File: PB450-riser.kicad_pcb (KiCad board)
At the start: 2 copper layers, 160 x 81.3 mm, 3 parts, among them J1 J1, J2 J2

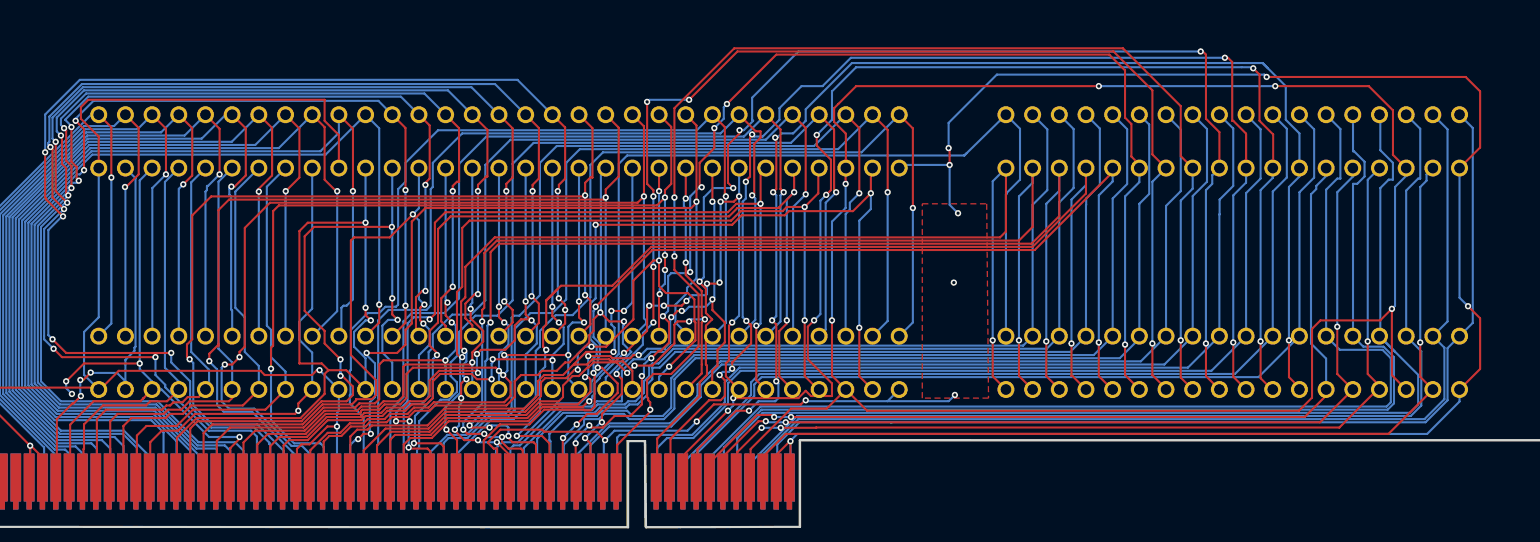
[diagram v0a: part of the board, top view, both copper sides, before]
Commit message: upload footprint for isa slot
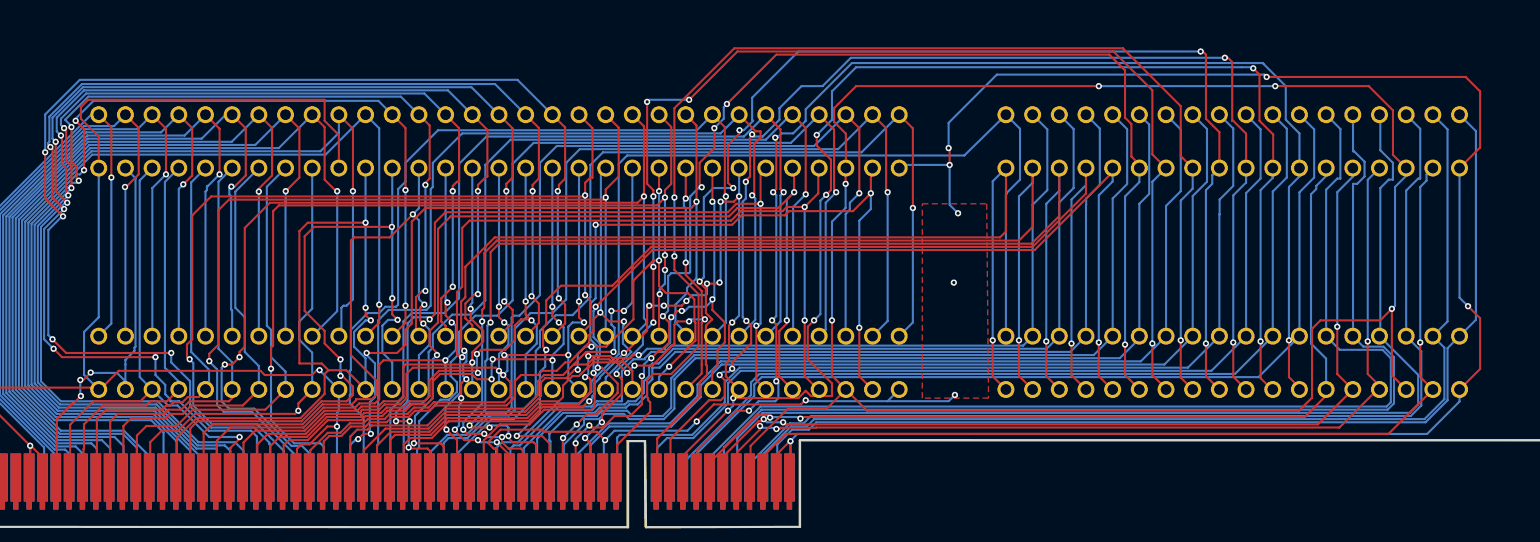
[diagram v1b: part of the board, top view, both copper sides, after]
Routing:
- net VCC: track 246.5 -> 237.4 mm, vias 9 -> 6
- net (no net): track 7616.4 -> 7612.3 mm, vias 242 -> 239

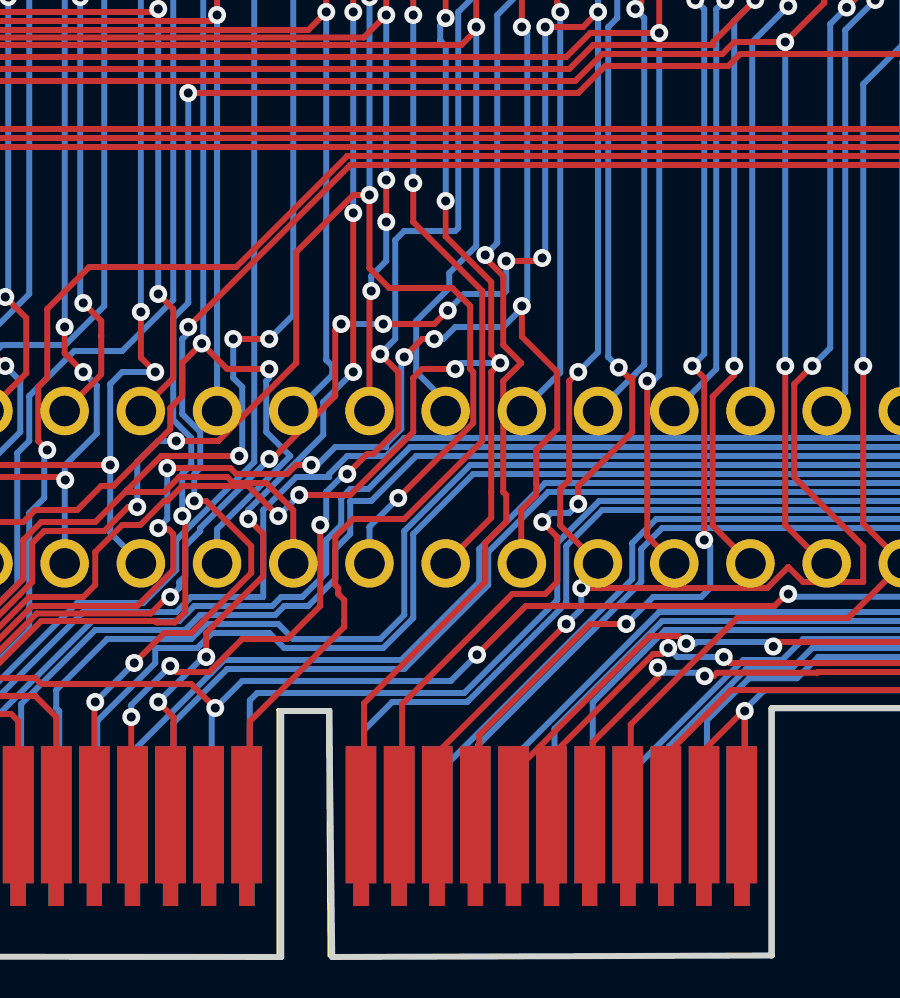
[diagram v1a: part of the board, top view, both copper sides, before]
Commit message: correcting for DRC
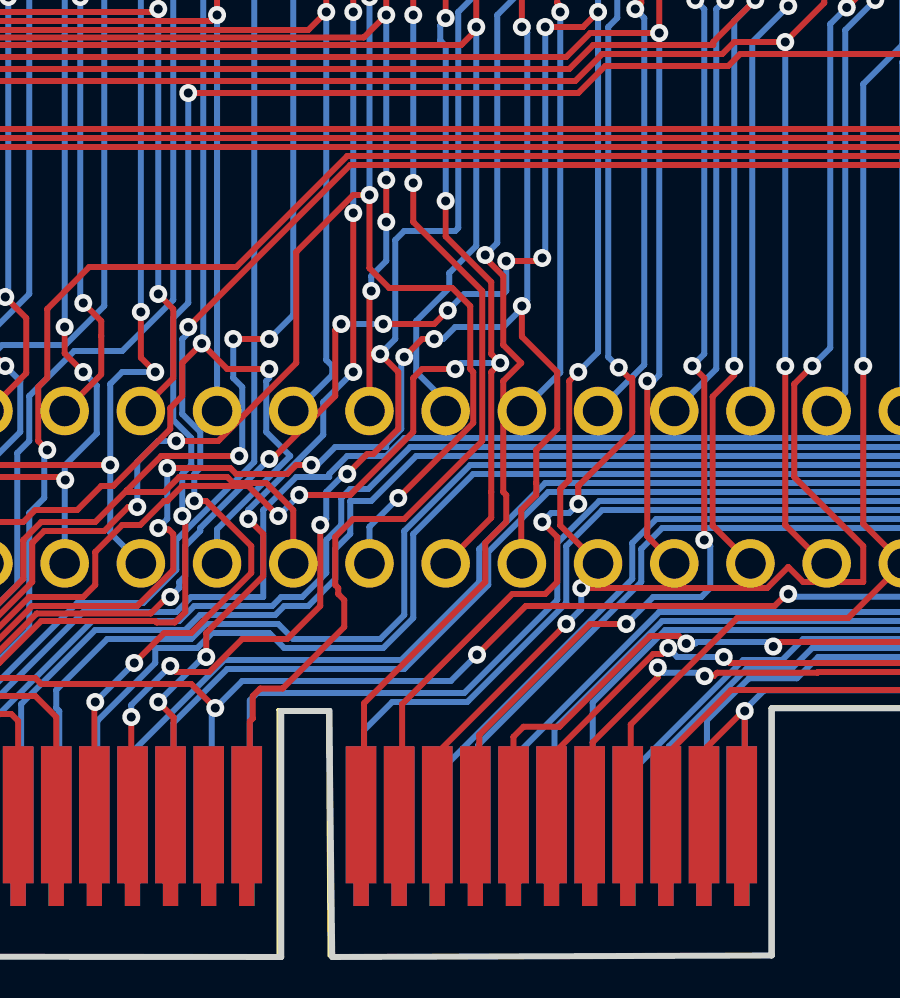
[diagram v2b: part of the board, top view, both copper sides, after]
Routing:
- net (no net): track 7612.3 -> 7615.0 mm

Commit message: revisions and adding foot prints
revisions and adding footprints
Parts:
- added P2: PCI 32bit footprint (partial), Connector_PCBEdge:BUS_PCI, F.Cu at (139.3, 92.7)
- J2: value J2 -> J1
- P1: renamed from REF**; value BUS_PCI -> ISA Bus over PCI; footprint Connector_PCBEdge:BUS_PCI -> Connector_PCBEdge:BUS_ISA-over-PCI
- moved J2 8.92 mm to (108.0, 116.6)
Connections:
- J1 pad A1: (no net) -> Net-(J1-~{IO_CH_CK})
- J1 pad A10: (no net) -> Net-(J1-IO_CH_RDY)
- J1 pad A11: (no net) -> Net-(J1-AEN)
- J1 pad A12: (no net) -> /SA19
- J1 pad A13: (no net) -> /SA18
- J1 pad A14: (no net) -> /SA17
- J1 pad A15: (no net) -> /SA16
- J1 pad A16: (no net) -> /SA15
- J1 pad A17: (no net) -> /SA14
- J1 pad A18: (no net) -> /SA13
- J1 pad A19: (no net) -> /SA12
- J1 pad A2: (no net) -> /SD7
- J1 pad A20: (no net) -> /SA11
- J1 pad A21: (no net) -> /SA10
- J1 pad A22: (no net) -> /SA9
- J1 pad A23: (no net) -> /SA8
- J1 pad A24: (no net) -> /SA7
- J1 pad A25: (no net) -> /SA6
- J1 pad A26: (no net) -> /SA5
- J1 pad A27: (no net) -> /SA4
- J1 pad A28: (no net) -> /SA3
- J1 pad A29: (no net) -> /SA2
- J1 pad A3: (no net) -> /SD6
- J1 pad A30: (no net) -> /SA1
- J1 pad A31: (no net) -> /SA0
- J1 pad A4: (no net) -> /SD5
- J1 pad A5: (no net) -> /SD4
- J1 pad A6: (no net) -> /SD3
- J1 pad A7: (no net) -> /SD2
- J1 pad A8: (no net) -> /SD1
- J1 pad A9: (no net) -> /SD0
- J1 pad B11: (no net) -> Net-(J1-~{SMEMW})
- J1 pad B12: (no net) -> Net-(J1-~{SMEMR})
- J1 pad B13: (no net) -> Net-(J1-~{IOW})
- J1 pad B14: (no net) -> Net-(J1-~{IOR})
- J1 pad B15: (no net) -> Net-(J1-~{DACK3})
- J1 pad B16: (no net) -> Net-(J1-DRQ3)
- J1 pad B17: (no net) -> Net-(J1-~{DACK1})
- J1 pad B18: (no net) -> Net-(J1-DRQ1)
- J1 pad B19: (no net) -> Net-(J1-~{REFRESH})
- J1 pad B2: (no net) -> Net-(J1-RESETDRV)
- J1 pad B20: (no net) -> Net-(J1-SYSCLK)
- J1 pad B21: (no net) -> Net-(J1-IRQ7)
- J1 pad B22: (no net) -> Net-(J1-IRQ6)
- J1 pad B23: (no net) -> Net-(J1-IRQ5)
- J1 pad B24: (no net) -> Net-(J1-IRQ4)
- J1 pad B25: (no net) -> Net-(J1-IRQ3)
- J1 pad B26: (no net) -> Net-(J1-~{DACK2})
- J1 pad B27: (no net) -> Net-(J1-TC)
- J1 pad B28: (no net) -> Net-(J1-BALE)
- J1 pad B29: VCC -> +5V
- J1 pad B3: VCC -> +5V
- J1 pad B30: (no net) -> Net-(J1-OSC)
- J1 pad B4: (no net) -> Net-(J1-IRQ9)
- J1 pad B6: (no net) -> Net-(J1-DRQ2)
- J1 pad B8: (no net) -> Net-(J1-~{0WS})
- J2 pad A1: (no net) -> Net-(J1-~{IO_CH_CK})
- J2 pad A10: (no net) -> Net-(J1-IO_CH_RDY)
- J2 pad A11: (no net) -> Net-(J1-AEN)
- J2 pad A12: (no net) -> /SA19
- J2 pad A13: (no net) -> /SA18
- J2 pad A14: (no net) -> /SA17
- J2 pad A15: (no net) -> /SA16
- J2 pad A16: (no net) -> /SA15
- J2 pad A17: (no net) -> /SA14
- J2 pad A18: (no net) -> /SA13
- J2 pad A19: (no net) -> /SA12
- J2 pad A2: (no net) -> /SD7
- J2 pad A20: (no net) -> /SA11
- J2 pad A21: (no net) -> /SA10
- J2 pad A22: (no net) -> /SA9
- J2 pad A23: (no net) -> /SA8
- J2 pad A24: (no net) -> /SA7
- J2 pad A25: (no net) -> /SA6
- J2 pad A26: (no net) -> /SA5
- J2 pad A27: (no net) -> /SA4
- J2 pad A28: (no net) -> /SA3
- J2 pad A29: (no net) -> /SA2
- J2 pad A3: (no net) -> /SD6
- J2 pad A30: (no net) -> /SA1
- J2 pad A31: (no net) -> /SA0
- J2 pad A4: (no net) -> /SD5
- J2 pad A5: (no net) -> /SD4
- J2 pad A6: (no net) -> /SD3
- J2 pad A7: (no net) -> /SD2
- J2 pad A8: (no net) -> /SD1
- J2 pad A9: (no net) -> /SD0
- J2 pad B1: (no net) -> GND
- J2 pad B10: (no net) -> GND
- J2 pad B11: (no net) -> Net-(J1-~{SMEMW})
- J2 pad B12: (no net) -> Net-(J1-~{SMEMR})
- J2 pad B13: (no net) -> Net-(J1-~{IOW})
- J2 pad B14: (no net) -> Net-(J1-~{IOR})
- J2 pad B15: (no net) -> Net-(J1-~{DACK3})
- J2 pad B16: (no net) -> Net-(J1-DRQ3)
- J2 pad B17: (no net) -> Net-(J1-~{DACK1})
- J2 pad B18: (no net) -> Net-(J1-DRQ1)
- J2 pad B19: (no net) -> Net-(J1-~{REFRESH})
- J2 pad B2: (no net) -> Net-(J1-RESETDRV)
- J2 pad B20: (no net) -> Net-(J1-SYSCLK)
- J2 pad B21: (no net) -> Net-(J1-IRQ7)
- J2 pad B22: (no net) -> Net-(J1-IRQ6)
- J2 pad B23: (no net) -> Net-(J1-IRQ5)
- J2 pad B24: (no net) -> Net-(J1-IRQ4)
- J2 pad B25: (no net) -> Net-(J1-IRQ3)
- J2 pad B26: (no net) -> Net-(J1-~{DACK2})
- J2 pad B27: (no net) -> Net-(J1-TC)
- J2 pad B28: (no net) -> Net-(J1-BALE)
- J2 pad B29: VCC -> +5V
- J2 pad B3: VCC -> +5V
- J2 pad B30: (no net) -> Net-(J1-OSC)
- J2 pad B4: (no net) -> Net-(J1-IRQ9)
- J2 pad B6: (no net) -> Net-(J1-DRQ2)
- J2 pad B8: (no net) -> Net-(J1-~{0WS})
- P1 pad A1: (no net) -> Net-(J1-~{IO_CH_CK})
- P1 pad A10: (no net) -> Net-(J1-IO_CH_RDY)
- P1 pad A11: (no net) -> Net-(J1-AEN)
- P1 pad A12: (no net) -> /SA19
- P1 pad A13: (no net) -> /SA18
- P1 pad A14: (no net) -> /SA17
- P1 pad A15: (no net) -> /SA16
- P1 pad A16: (no net) -> /SA15
- P1 pad A17: (no net) -> /SA14
- P1 pad A18: (no net) -> /SA13
- P1 pad A19: (no net) -> /SA12
- P1 pad A2: (no net) -> /SD7
- P1 pad A20: (no net) -> /SA11
- P1 pad A21: (no net) -> /SA10
- P1 pad A22: (no net) -> /SA9
- P1 pad A23: (no net) -> /SA8
- P1 pad A24: (no net) -> /SA7
- P1 pad A25: (no net) -> /SA6
- P1 pad A26: (no net) -> /SA5
- P1 pad A27: (no net) -> /SA4
- P1 pad A28: GND -> /SA3
- P1 pad A29: (no net) -> /SA2
- P1 pad A3: (no net) -> /SD6
- P1 pad A30: (no net) -> /SA1
- P1 pad A31: (no net) -> /SA0
- P1 pad A4: (no net) -> /SD5
- P1 pad A5: GND -> /SD4
- P1 pad A6: (no net) -> /SD3
- P1 pad A7: (no net) -> /SD2
- P1 pad A8: (no net) -> /SD1
- P1 pad A9: (no net) -> /SD0
- P1 pad B1: (no net) -> GND
- P1 pad B10: -5V -> GND
- P1 pad B11: (no net) -> Net-(J1-~{SMEMW})
- P1 pad B12: -12V -> Net-(J1-~{SMEMR})
- P1 pad B13: (no net) -> Net-(J1-~{IOW})
- P1 pad B14: +12V -> Net-(J1-~{IOR})
- P1 pad B15: (no net) -> Net-(J1-~{DACK3})
- P1 pad B16: (no net) -> Net-(J1-DRQ3)
- P1 pad B17: (no net) -> Net-(J1-~{DACK1})
- P1 pad B18: (no net) -> Net-(J1-DRQ1)
- P1 pad B2: (no net) -> Net-(J1-RESETDRV)
- P1 pad B20: VCC -> Net-(J1-~{REFRESH})
- P1 pad B21: (no net) -> Net-(J1-SYSCLK)
- P1 pad B22: (no net) -> Net-(J1-IRQ7)
- P1 pad B23: (no net) -> Net-(J1-IRQ6)
- P1 pad B24: (no net) -> Net-(J1-IRQ5)
- P1 pad B25: GND -> Net-(J1-IRQ4)
- P1 pad B26: (no net) -> Net-(J1-IRQ3)
- P1 pad B27: (no net) -> Net-(J1-~{DACK2})
- P1 pad B28: (no net) -> Net-(J1-TC)
- P1 pad B29: (no net) -> +5V
- P1 pad B3: (no net) -> +5V
- P1 pad B30: (no net) -> Net-(J1-OSC)
- P1 pad B31: (no net) -> GND
- P1 pad B4: (no net) -> Net-(J1-IRQ9)
- P1 pad B5: GND -> -5V
- P1 pad B6: GND -> Net-(J1-DRQ2)
- P1 pad B7: (no net) -> -12V
- P1 pad B8: VCC -> Net-(J1-~{0WS})
- P1 pad B9: (no net) -> +12V
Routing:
- net (no net): track 7615.0 -> 0.00 mm, vias 239 -> 0
- net +5V: track 0.00 -> 342.5 mm, vias 0 -> 7
- net VCC: track 237.4 -> 0.00 mm, vias 6 -> 0
- net /SA18: track 0.00 -> 134.2 mm, vias 0 -> 3
- net /SA19: track 0.00 -> 129.0 mm, vias 0 -> 1
- net /SD15: track 0.00 -> 128.7 mm, vias 0 -> 2
- net /SD14: track 0.00 -> 128.3 mm, vias 0 -> 2
- net Net-(J1-IO_CH_RDY): track 0.00 -> 127.9 mm, vias 0 -> 1
- net Net-(J1-AEN): track 0.00 -> 126.9 mm, vias 0 -> 1
- net /SD13: track 0.00 -> 124.2 mm, vias 0 -> 2
- net /SD12: track 0.00 -> 122.5 mm, vias 0 -> 2
- net /SD11: track 0.00 -> 120.6 mm, vias 0 -> 2
- net /SD0: track 0.00 -> 119.5 mm, vias 0 -> 1
- net /SD10: track 0.00 -> 118.6 mm, vias 0 -> 2
- net /SD9: track 0.00 -> 116.0 mm, vias 0 -> 2
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- removed copper zone on F.Cu, net GND

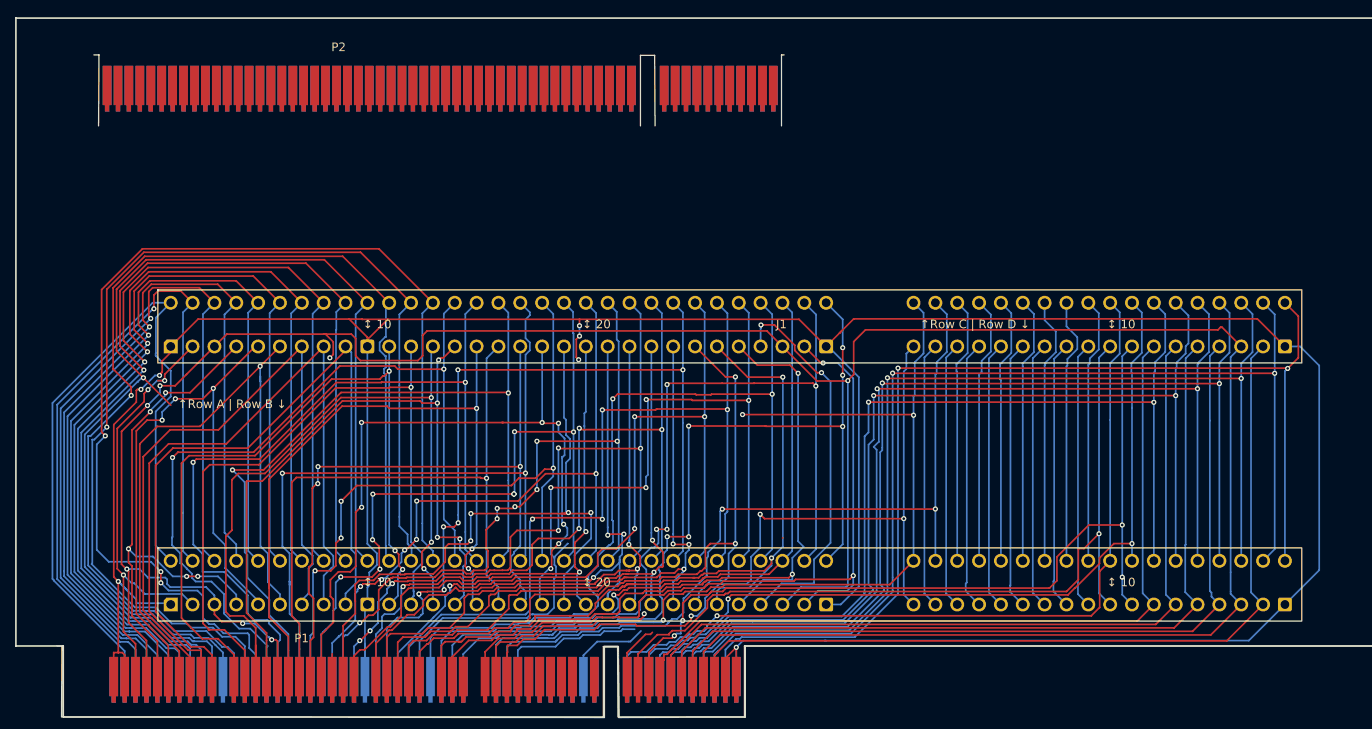
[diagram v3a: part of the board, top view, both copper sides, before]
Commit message: added third slot and gerber files
added third slot and gerber files
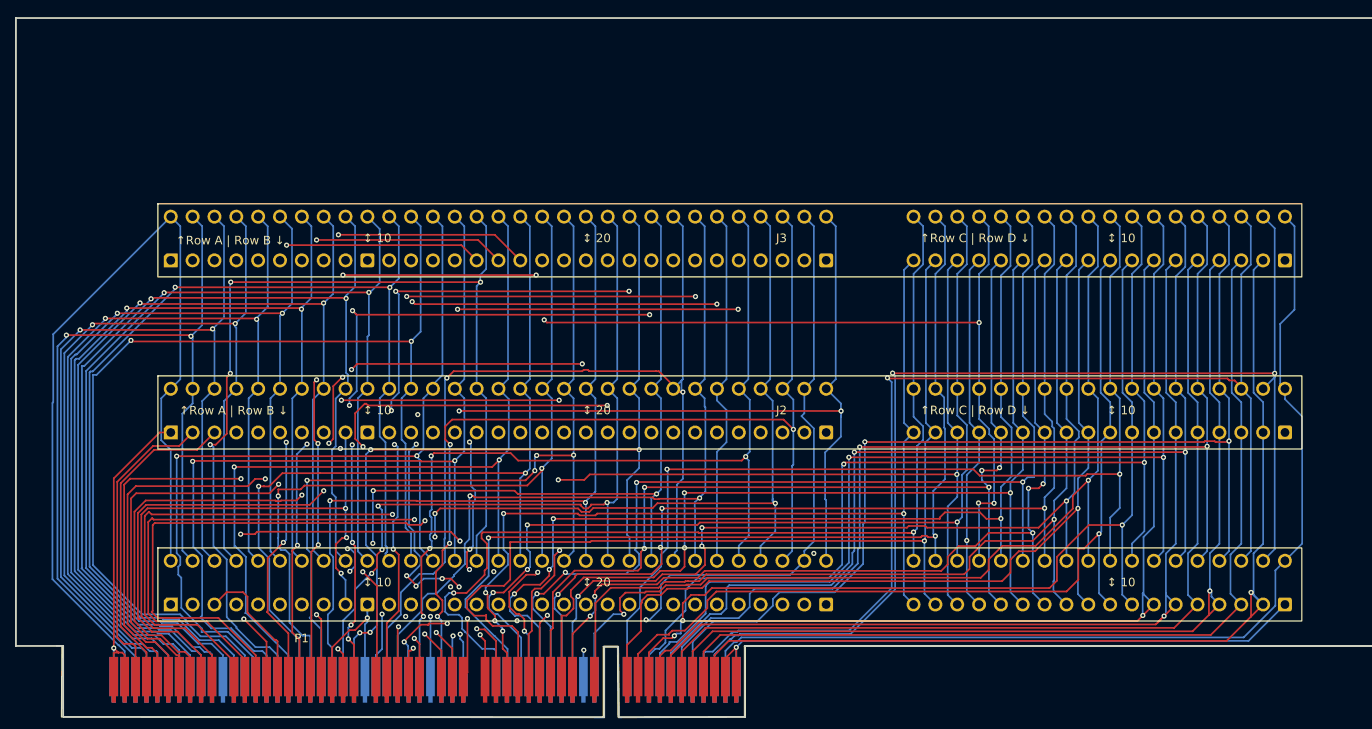
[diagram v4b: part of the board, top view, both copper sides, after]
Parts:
- removed P2: PCI 32bit footprint (partial), Connector_PCBEdge:BUS_PCI
- added J3: J3, Connector:ISA_Mount_Holes, F.Cu at (108.0, 106.6)
- J2: value J1 -> J2
- moved J2 10.0 mm to (108.0, 126.6)
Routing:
- net GND: track 427.4 -> 613.5 mm, vias 8 -> 5
- net +5V: track 342.5 -> 486.3 mm, vias 7 -> 6
- net /LA21: track 31.1 -> 140.4 mm, vias 0 -> 6
- net /LA19: track 31.1 -> 121.4 mm, vias 0 -> 4
- net /LA20: track 31.1 -> 118.6 mm, vias 0 -> 4
- net /LA18: track 31.1 -> 116.6 mm, vias 0 -> 4
- net /LA17: track 31.0 -> 116.3 mm, vias 0 -> 4
- net Net-(J1-~{MEMR}): track 31.0 -> 115.0 mm, vias 0 -> 2
- net Net-(J1-IRQ12): track 31.2 -> 114.7 mm, vias 0 -> 5
- net Net-(J1-~{IOCS16}): track 31.1 -> 114.1 mm, vias 0 -> 1
- net Net-(J1-IRQ15): track 31.2 -> 114.0 mm, vias 0 -> 3
- net Net-(J1-IRQ10): track 31.1 -> 113.3 mm, vias 0 -> 3
- net Net-(J1-~{DACK0}): track 31.3 -> 108.9 mm, vias 0 -> 1
- net Net-(J1-IRQ14): track 31.1 -> 108.5 mm, vias 0 -> 5
- net Net-(J1-IRQ11): track 31.3 -> 103.8 mm, vias 0 -> 2
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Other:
- copper layers 2 -> 4

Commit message: Added capacitors and trace optimization
Added capacitors and trace optimization
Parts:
- added C1: 22uF 25V, Capacitor_THT:CP_Radial_D5.0mm_P2.00mm, F.Cu at (97.7, 145.5)
- added C10: 104K, Capacitor_THT:C_Disc_D5.0mm_W2.5mm_P2.50mm, F.Cu at (121.4, 89.5)
- added C11: 22uF 25V, Capacitor_THT:CP_Radial_D5.0mm_P2.00mm, F.Cu at (130.0, 98.4)
- added C12: 104K, Capacitor_THT:C_Disc_D5.0mm_W2.5mm_P2.50mm, F.Cu at (129.7, 89.5)
- added C13: 104K, Capacitor_THT:C_Disc_D5.0mm_W2.5mm_P2.50mm, F.Cu at (187.6, 151.8)
- added C14: 104K, Capacitor_THT:C_Disc_D5.0mm_W2.5mm_P2.50mm, F.Cu at (187.7, 126.9)
- added C15: 104K, Capacitor_THT:C_Disc_D5.0mm_W2.5mm_P2.50mm, F.Cu at (188.8, 116.5)
- added C16: 104K, Capacitor_THT:C_Disc_D5.0mm_W2.5mm_P2.50mm, F.Cu at (176.0, 99.6)
- added C17: 22uF 25V, Capacitor_THT:CP_Radial_D5.0mm_P2.00mm, F.Cu at (184.9, 99.6)
- added C18: 22uF 25V, Capacitor_THT:CP_Radial_D5.0mm_P2.00mm, F.Cu at (203.2, 99.7)
- added C19: 104K, Capacitor_THT:C_Disc_D5.0mm_W2.5mm_P2.50mm, F.Cu at (240.8, 119.3)
- added C2: 22uF 25V, Capacitor_THT:CP_Radial_D5.0mm_P2.00mm, F.Cu at (96.0, 102.7)
- added C20: 22uF 25V, Capacitor_THT:CP_Radial_D5.0mm_P2.00mm, F.Cu at (234.1, 98.1)
- added C21: 22uF 25V, Capacitor_THT:CP_Radial_D5.0mm_P2.00mm, F.Cu at (243.0, 136.4)
- added C22: 104K, Capacitor_THT:C_Disc_D5.0mm_W2.5mm_P2.50mm, F.Cu at (241.4, 124.1)
- added C23: 104K, Capacitor_THT:C_Disc_D5.0mm_W2.5mm_P2.50mm, F.Cu at (242.8, 142.2)
- added C3: 104K, Capacitor_THT:C_Disc_D5.0mm_W2.5mm_P2.50mm, F.Cu at (102.5, 95.3)
- added C4: 104K, Capacitor_THT:C_Disc_D5.0mm_W2.5mm_P2.50mm, F.Cu at (100.8, 131.0)
- added C5: 104K, Capacitor_THT:C_Disc_D5.0mm_W2.5mm_P2.50mm, F.Cu at (117.2, 142.4)
- added C6: 104K, Capacitor_THT:C_Disc_D5.0mm_W2.5mm_P2.50mm, F.Cu at (103.6, 115.9)
- added C7: 22uF 25V, Capacitor_THT:CP_Radial_D5.0mm_P2.00mm, F.Cu at (112.5, 98.4)
- added C8: 104K, Capacitor_THT:C_Disc_D5.0mm_W2.5mm_P2.50mm, F.Cu at (112.2, 89.5)
- added C9: 22uF 25V, Capacitor_THT:CP_Radial_D5.0mm_P2.00mm, F.Cu at (121.7, 98.4)
- J2: value J2 -> J1
- J3: value J3 -> J1
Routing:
- net +5V: track 486.3 -> 779.9 mm, vias 6 -> 12
- net GND: track 613.5 -> 856.7 mm, vias 5 -> 12
- net /SA13: track 97.8 -> 138.5 mm, vias 2 -> 7
- net /SA14: track 97.8 -> 134.1 mm, vias 2 -> 4
- net -5V: track 82.4 -> 114.7 mm, vias 1 -> 0
- net Net-(J1-IO_CH_RDY): track 124.4 -> 96.1 mm
- net Net-(J1-AEN): track 126.7 -> 101.2 mm, vias 2 -> 4
- net -12V: track 85.4 -> 108.4 mm
- net Net-(J1-~{SMEMR}): track 97.6 -> 120.6 mm, vias 1 -> 3
- net /SA17: track 103.1 -> 121.4 mm, vias 2 -> 6
- net /SA19: track 127.3 -> 112.1 mm, vias 2 -> 4
- net Net-(J1-~{IOW}): track 101.8 -> 87.9 mm, vias 1 -> 3
- net /SD0: track 121.5 -> 114.9 mm
- net /SD1: track 118.3 -> 114.9 mm
- net /SD2: track 115.5 -> 112.7 mm
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
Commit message: added mounting holes for affixing PCB in frame of computer
added mounting holes for affixing PCB in frame of computer
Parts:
- added REF**: MountingHole_3.7mm_Pad, MountingHole:MountingHole_3.7mm_Pad, F.Cu at (95.8, 89.3)
- added REF**: MountingHole_3.7mm_Pad, MountingHole:MountingHole_3.7mm_Pad, F.Cu at (244.2, 89.3)
